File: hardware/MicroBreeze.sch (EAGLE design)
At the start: 41 parts, among them IC1 OPA2251UA, IC3 LM2941TO220-V, IC4 LM2941TO220-V, IC5 ATMEGA328P, J1 COMPUTER-PERIPHERAL-POWERVERT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, Y1 16MHZ

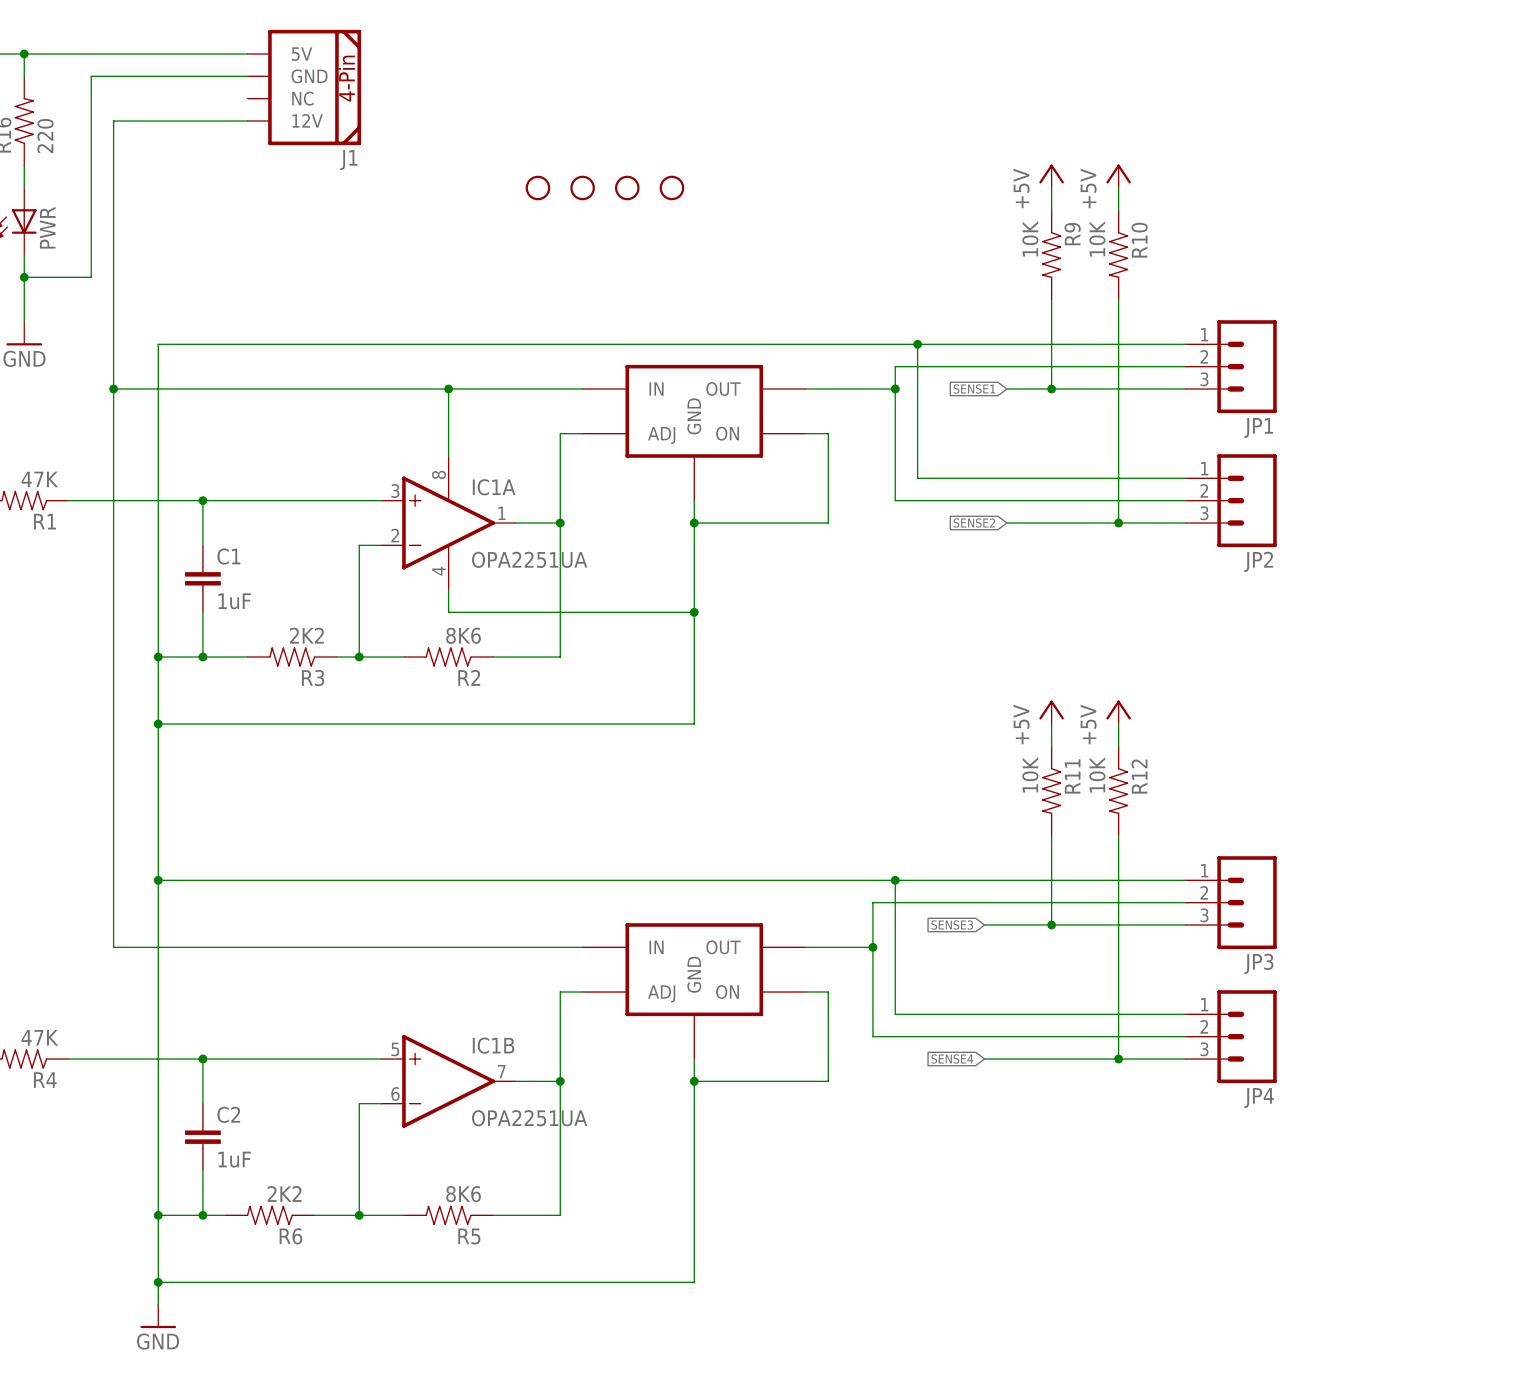
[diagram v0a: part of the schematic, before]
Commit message: Add filter caps
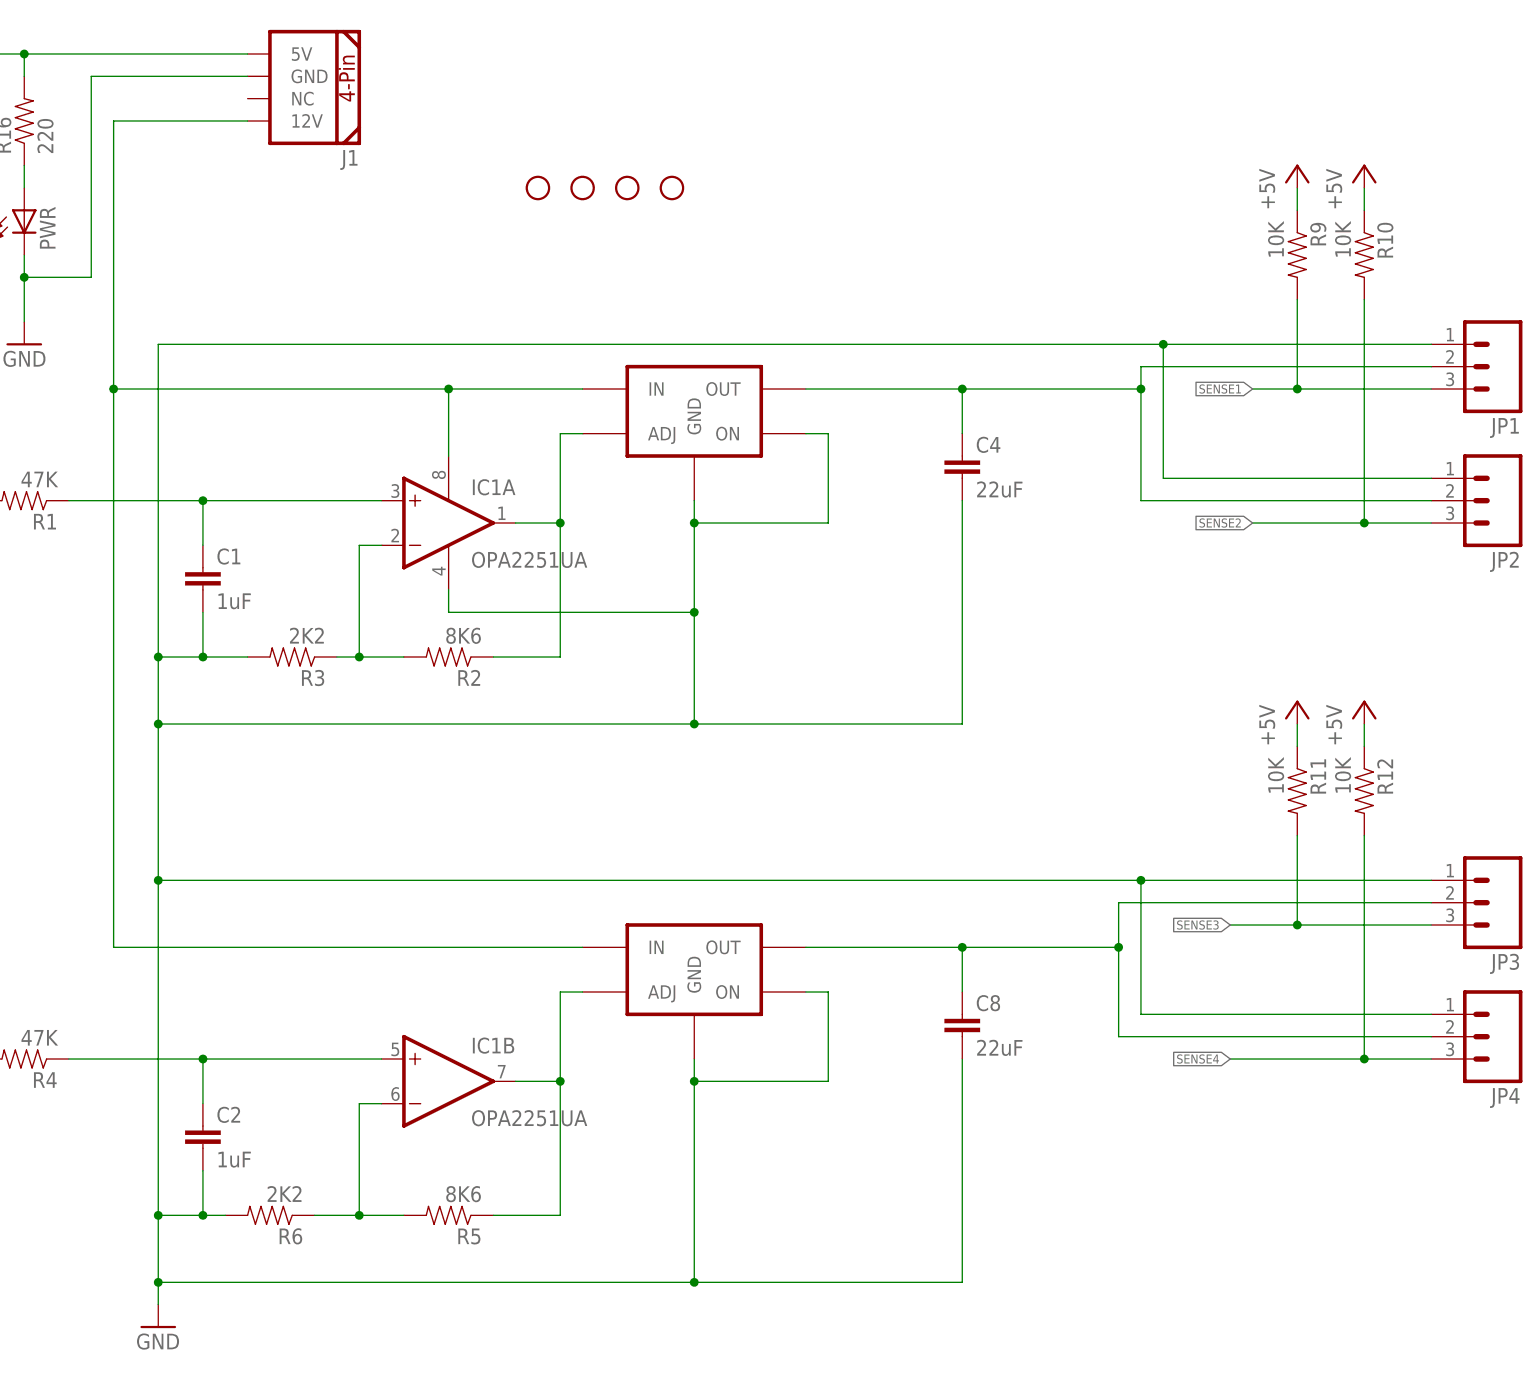
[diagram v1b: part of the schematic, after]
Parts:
- added C4, C8: 22uF, SparkFun-Capacitors:22UF-16V-20%-(1210)
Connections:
- net GND: now also C4.2, C8.2
- net N$13: now also C8.1
- net N$8: now also C4.1
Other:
- moved on the sheet: JP1, JP2, JP3, JP4, R10, R11, R12, R9

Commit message: Board updates
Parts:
- added R17, R8: 240, SparkFun-Resistors:RESISTOR0805-RES
- C4, C8: value 22uF -> 47uF; device SparkFun-Capacitors:22UF-16V-20%-(1210) -> SparkFun-Capacitors:47UF-TANT
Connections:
- removed net N$14: IC1B.OUT, IC4.ADJ, R5.1
- new net N$19: IC1B.OUT, IC4.ADJ, R5.1, R8.1
- net GND: now also C4.-, C8.-; no longer C4.2, C8.2
- net N$13: now also C8.+, R8.2; no longer C8.1
- net N$2: now also R17.1
- net N$8: now also C4.+, R17.2; no longer C4.1
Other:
- moved on the sheet: C1, C2, IC1A, IC1B, JP1, JP2, JP3, JP4, R1, R10, R11, R12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
